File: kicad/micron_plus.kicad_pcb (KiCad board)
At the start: 2 copper layers, 163.8 x 123.2 mm, 90 parts, among them J1 Conn_02x17_Odd_Even, J2 Cliff DC10A, Q1 2N2905A, Q2 2N2905A, Q3 2N3904, Q4 2N3904, U1 MC68A21, U10 74LS00, U11 7406, U12 HM6264LP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

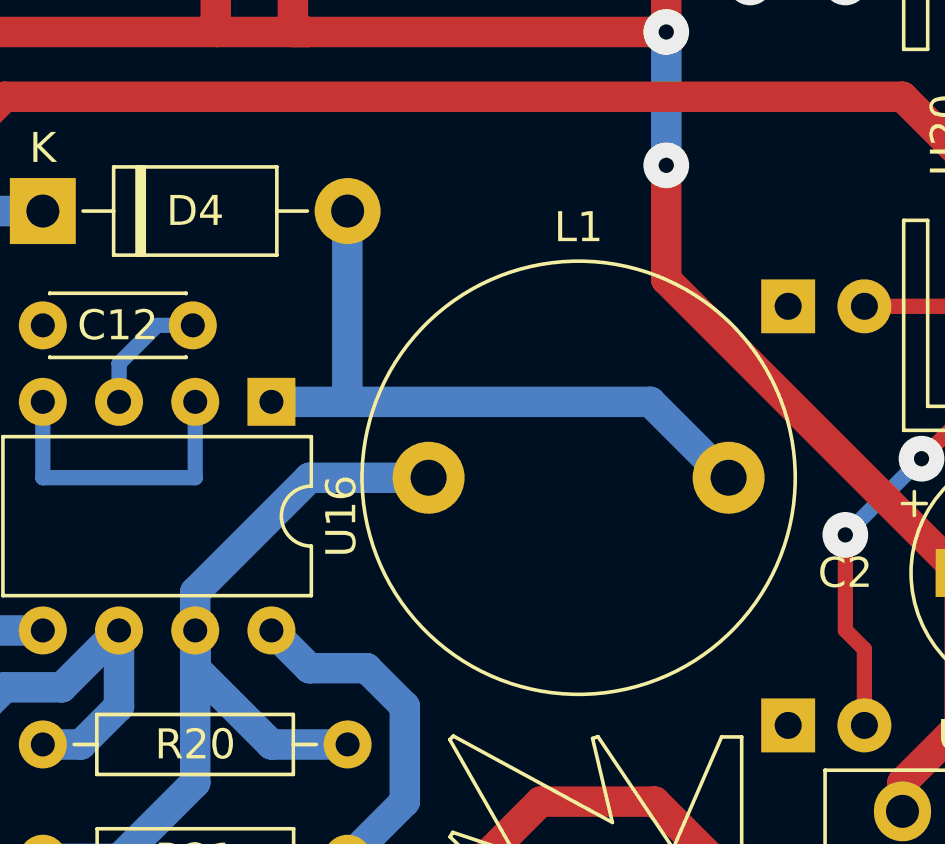
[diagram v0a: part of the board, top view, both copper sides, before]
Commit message: KiCAD: Custom footprint for inductor with multiple pads
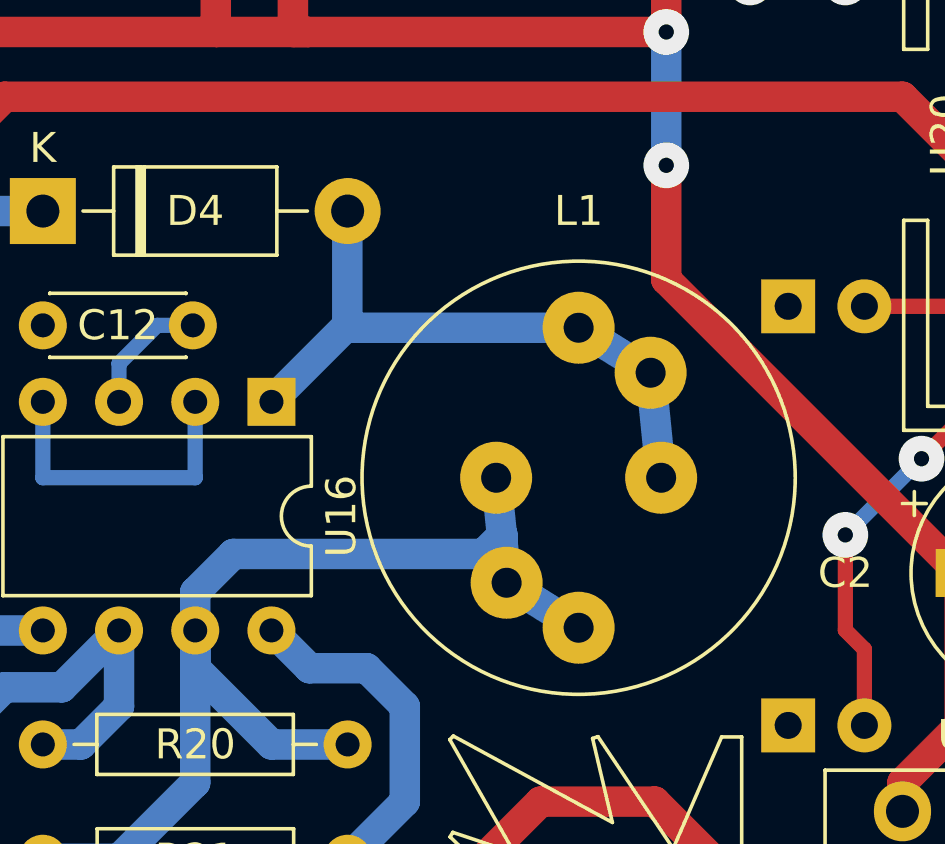
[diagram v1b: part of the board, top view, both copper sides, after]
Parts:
- L1: footprint Inductor_THT:L_Radial_D14.2mm_P10.00mm_Neosid_SD14 -> custom_footprints:L_Radial_D14.2mm_P10.00mm_Kemet
- moved L1 7.07 mm to (159.4, 127.6), turned to 90 degrees
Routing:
- net Net-(L1-Pad1): track 29.2 -> 38.7 mm
- net Net-(D4-Pad2): track 22.6 -> 21.5 mm
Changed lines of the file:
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@@
     )
   )
-  (footprint "Inductor_THT:L_Radial_D14.2mm_P10.00mm_Neosid_SD14" (layer "F.Cu")
-    (at 154.385 122.555)
+  (footprint "custom_footprints:L_Radial_D14.2mm_P10.00mm_Kemet" (layer "F.Cu")
+    (at 159.385 127.555 90)
     (descr "Inductor, Radial series, Radial, pin pitch=10.00mm, , diameter=14.2mm, Neosid, SD14, http://www.neosid.de/produktblaetter/neosid_Festinduktivitaet_Sd14.pdf")
     (tags "Inductor Radial series Radial pin pitch 10.00mm  diameter 14.2mm Neosid SD14")
@@
     (property "Sheetname" "Power Supply")
     (attr through_hole)
-    (fp_text reference "L1" (at 5 -8.35) (layer "F.SilkS")
+    (fp_text reference "L1" (at 13.89 0 180) (layer "F.SilkS")
       (effects (font (size 1 1) (thickness 0.15)))
     )
-    (fp_text value "220uH" (at 5 8.35) (layer "F.Fab")
+    (fp_text value "220uH" (at 5 8.35 90) (layer "F.Fab")
       (effects (font (size 1 1) (thickness 0.15)))
     )
-    (fp_text user "${REFERENCE}" (at 5 0) (layer "F.Fab")
+    (fp_text user "${REFERENCE}" (at 5 -5 90) (layer "F.Fab")
       (effects (font (size 1 1) (thickness 0.15)))
     )
@@
     (fp_circle (center 5 0) (end 12.35 0) (layer "F.CrtYd") (width 0.05) (fill none))
     (fp_circle (center 5 0) (end 12.1 0) (layer "F.Fab") (width 0.1) (fill none))
-    (pad "1" thru_hole circle (at 0 0) (size 2.4 2.4) (drill 1.2) (layers *.Cu *.Mask)
+    (pad "1" thru_hole circle (at 1.5 -2.4 90) (size 2.4 2.4) (drill 1) (layers *.Cu *.Mask)
       (net 174 "Net-(L1-Pad1)") (pinfunction "1") (pintype "passive"))
-    (pad "2" thru_hole circle (at 10 0) (size 2.4 2.4) (drill 1.2) (layers *.Cu *.Mask)
+    (pad "1" thru_hole circle (at 5 -2.75 90) (size 2.4 2.4) (drill 1) (layers *.Cu *.Mask)
+      (net 174 "Net-(L1-Pad1)") (pinfunction "1") (pintype "passive"))
+    (pad "1" thru_hole circle (at 0 0 90) (size 2.4 2.4) (drill 1) (layers *.Cu *.Mask)
+      (net 174 "Net-(L1-Pad1)") (pinfunction "1") (pintype "passive"))
+    (pad "2" thru_hole circle (at 10 0 90) (size 2.4 2.4) (drill 1) (layers *.Cu *.Mask)
+      (net 173 "Net-(D4-Pad2)") (pinfunction "2") (pintype "passive"))
+    (pad "2" thru_hole circle (at 5 2.75 90) (size 2.4 2.4) (drill 1) (layers *.Cu *.Mask)
+      (net 173 "Net-(D4-Pad2)") (pinfunction "2") (pintype "passive"))
+    (pad "2" thru_hole circle (at 8.5 2.4 90) (size 2.4 2.4) (drill 1) (layers *.Cu *.Mask)
       (net 173 "Net-(D4-Pad2)") (pinfunction "2") (pintype "passive"))
     (model "${KICAD6_3DMODEL_DIR}/Inductor_THT.3dshapes/L_Radial_D14.2mm_P10.00mm_Neosid_SD14.wrl"
@@
   (segment (start 77.724 33.528) (end 81.026 36.83) (width 0.508) (layer "B.Cu") (net 169))
   (segment (start 58.928 35.56) (end 58.928 35.052) (width 0.508) (layer "B.Cu") (net 169))
-  (segment (start 151.675 120.025) (end 151.675 113.675) (width 1.016) (layer "B.Cu") (net 173))
-  (segment (start 149.145 120.025) (end 151.675 120.025) (width 1.016) (layer "B.Cu") (net 173))
-  (segment (start 151.675 120.025) (end 161.775 120.025) (width 1.016) (layer "B.Cu") (net 173))
-  (segment (start 161.775 120.025) (end 164.305 122.555) (width 1.016) (layer "B.Cu") (net 173))
-  (segment (start 146.605 126.365) (end 146.605 127.645) (width 1.016) (layer "B.Cu") (net 174))
+  (segment (start 159.385 117.555) (end 151.755 117.555) (width 1.016) (layer "B.Cu") (net 173))
+  (segment (start 162.135 122.555) (end 161.785 119.055) (width 1.016) (layer "B.Cu") (net 173))
+  (segment (start 149.145 120.005) (end 151.675 117.475) (width 1.016) (layer "B.Cu") (net 173))
+  (segment (start 159.385 117.555) (end 161.785 119.055) (width 1.016) (layer "B.Cu") (net 173))
+  (segment (start 151.675 117.475) (end 151.675 113.675) (width 1.016) (layer "B.Cu") (net 173))
+  (segment (start 151.755 117.555) (end 151.675 117.475) (width 1.016) (layer "B.Cu") (net 173))
+  (segment (start 156.21 125.095) (end 156.845 124.46) (width 1.016) (layer "B.Cu") (net 174))
+  (segment (start 156.845 124.46) (end 156.845 125.915) (width 1.016) (layer "B.Cu") (net 174))
   (segment (start 146.605 127.645) (end 146.605 132.715) (width 1.016) (layer "B.Cu") (net 174))
   (segment (start 149.145 131.445) (end 146.605 128.905) (width 1.016) (layer "B.Cu") (net 174))
-  (segment (start 154.385 122.555) (end 150.415 122.555) (width 1.016) (layer "B.Cu") (net 174))
+  (segment (start 146.605 127.645) (end 146.605 126.365) (width 1.016) (layer "B.Cu") (net 174))
+  (segment (start 156.635 122.555) (end 156.985 126.055) (width 1.016) (layer "B.Cu") (net 174))
   (segment (start 144.065 135.255) (end 141.525 135.255) (width 1.016) (layer "B.Cu") (net 174))
-  (segment (start 150.415 122.555) (end 146.605 126.365) (width 1.016) (layer "B.Cu") (net 174))
   (segment (start 151.685 131.445) (end 149.145 131.445) (width 1.016) (layer "B.Cu") (net 174))
   (segment (start 146.605 128.905) (end 146.605 127.635) (width 1.016) (layer "B.Cu") (net 174))
+  (segment (start 147.875 125.095) (end 156.21 125.095) (width 1.016) (layer "B.Cu") (net 174))
+  (segment (start 146.605 126.365) (end 147.875 125.095) (width 1.016) (layer "B.Cu") (net 174))
+  (segment (start 156.985 126.055) (end 159.385 127.555) (width 1.016) (layer "B.Cu") (net 174))
   (segment (start 146.605 132.715) (end 144.065 135.255) (width 1.016) (layer "B.Cu") (net 174))
   (segment (start 191.77 71.11) (end 191.77 68.57) (width 0.508) (layer "F.Cu") (net 175))
@@
   (segment (start 189.23 93.345) (end 187.96 92.075) (width 0.508) (layer "B.Cu") (net 182))
   (zone (net 2) (net_name "GND") (layer "B.Cu") (hatch edge 0.508)
-    (connect_pads (clearance 1.27))
+    (connect_pads (clearance 1.016))
     (min_thickness 0.508) (filled_areas_thickness no)
     (fill yes (thermal_gap 0.508) (thermal_bridge_width 0.508))

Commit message: KiCAD - silk screen
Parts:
- C11, C13: value 100u/50V -> 100u
- C15: value 4.7u/35V -> 4u7
- C2: value 220u/16V -> 220u
- C8: value 10u/35V -> 10u
- C9: value 100u/16V -> 100u
- U18: value LM7805_TO220 -> LM7805
- U19, U20: value LM317SP_TO220 -> LM317T
- moved C15 0.71 mm to (185.4, 85.7)
- moved R20 0.64 mm to (141.5, 132.1)
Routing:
- net Net-(C15-Pad1): track 67.1 -> 65.4 mm
- net Net-(C16-Pad1): track 58.2 -> 56.7 mm
- net Net-(U10-Pad4): track 133.4 -> 134.7 mm
- net GND: track 681.7 -> 682.7 mm
- net /Main Logic and Eprom Socket/EpromVPP: track 180.0 -> 179.1 mm
- net /Control Latches/n2564Mode: track 127.3 -> 126.7 mm
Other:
- board text added: "16V"
- board text added: "35V"
- board text added: "50V"
- board text added: "9VDC Centre+"

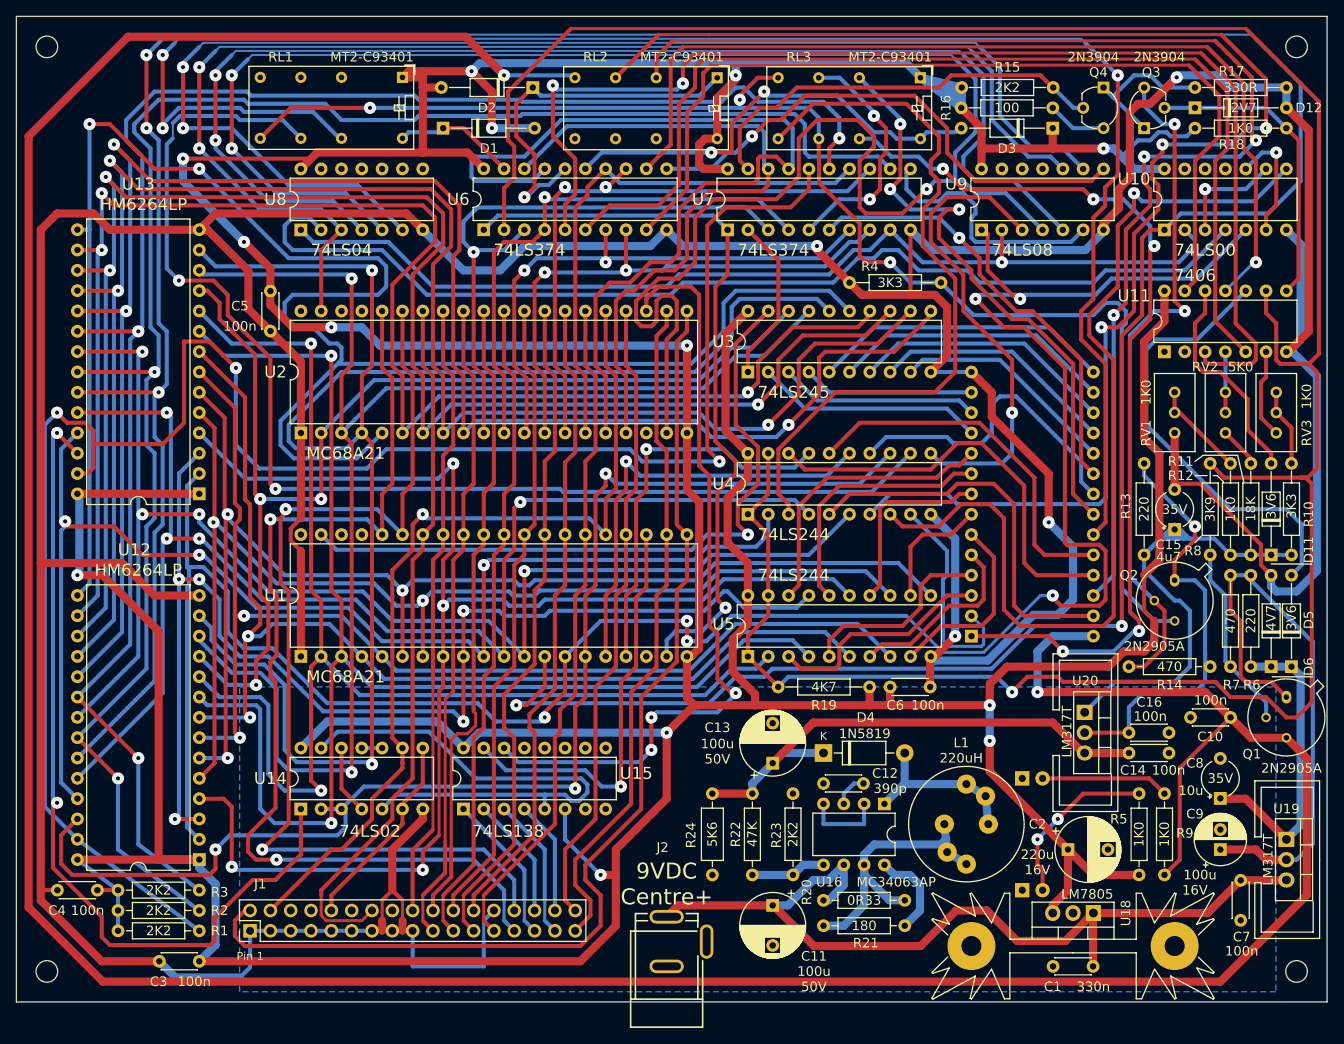
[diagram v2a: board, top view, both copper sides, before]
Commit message: KiCAD - more silk screen
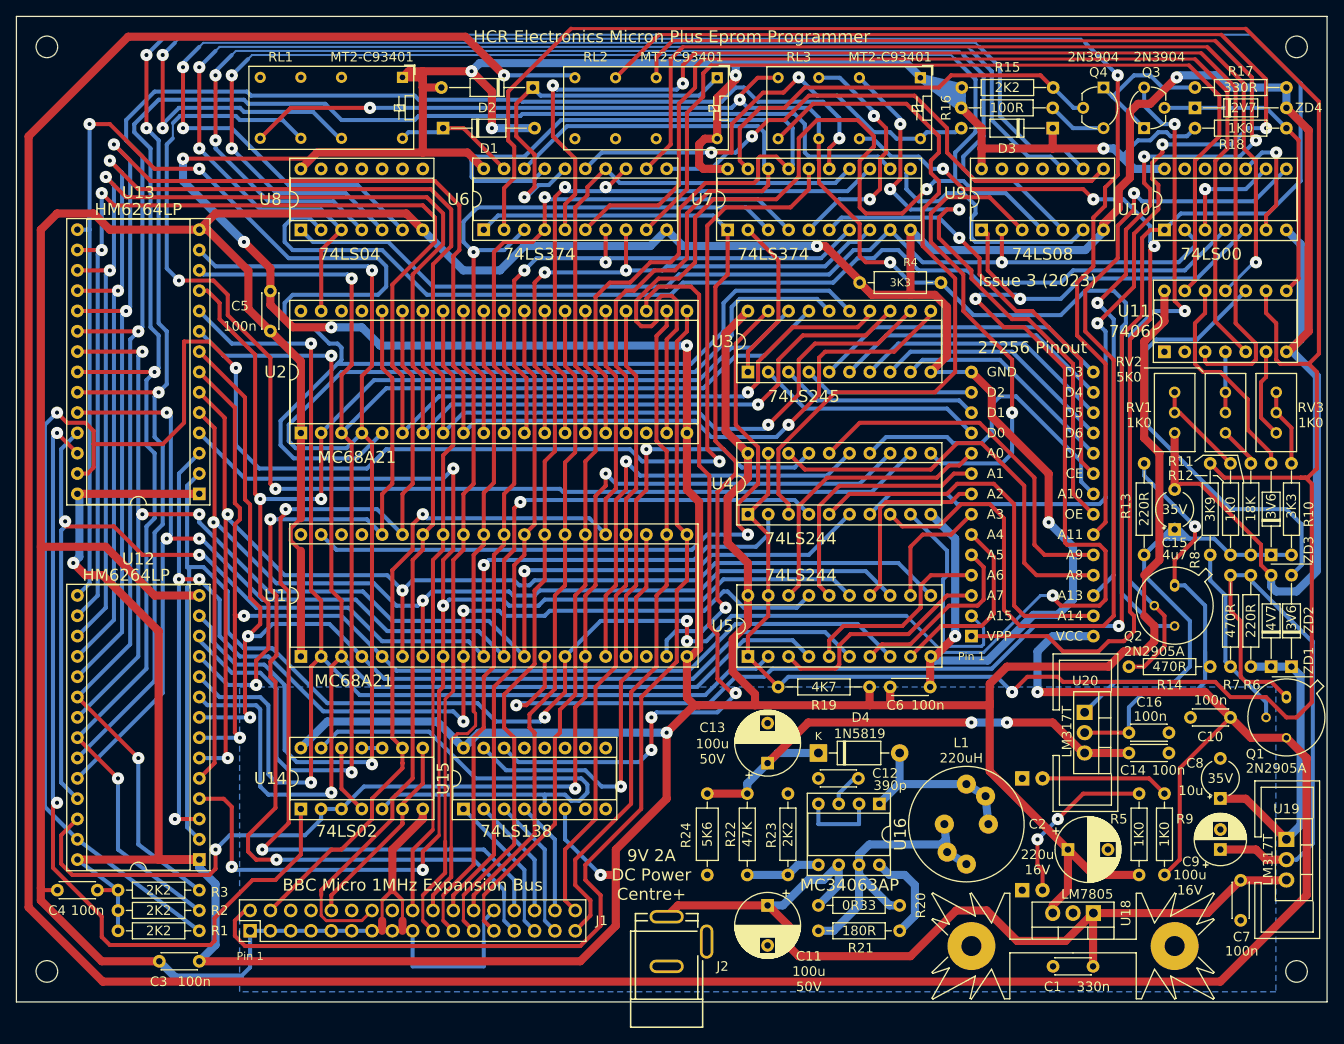
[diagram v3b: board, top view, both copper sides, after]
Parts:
- R13, R6: value 220 -> 220R
- R14, R7: value 470 -> 470R
- R16: value 100 -> 100R
- R21: value 180 -> 180R
- R4: footprint custom_footprints:R_Axial_DIN0207_L6.3mm_D2.0mm_P11.43mm_Horizontal -> Resistor_THT:R_Axial_DIN0207_L6.3mm_D2.5mm_P10.16mm_Horizontal
- U1, U2: footprint Package_DIP:DIP-40_W15.24mm -> Package_DIP:DIP-40_W15.24mm_Socket
- U10, U11, U14, U8, U9: footprint Package_DIP:DIP-14_W7.62mm -> Package_DIP:DIP-14_W7.62mm_Socket
- U12, U13: footprint Package_DIP:DIP-28_W15.24mm -> Package_DIP:DIP-28_W15.24mm_Socket
- U15: footprint Package_DIP:DIP-16_W7.62mm -> Package_DIP:DIP-16_W7.62mm_Socket
- U16: footprint Package_DIP:DIP-8_W7.62mm -> Package_DIP:DIP-8_W7.62mm_Socket
- U3, U4, U5, U6, U7: footprint Package_DIP:DIP-20_W7.62mm -> Package_DIP:DIP-20_W7.62mm_Socket
- moved C12 0.90 mm to (145.9, 116.8)
- moved R20 0.90 mm to (140.9, 132.7)
- moved R21 0.90 mm to (151.1, 135.9)
- moved C11 0.64 mm to (134.5, 132.7)
- moved C13 0.64 mm to (134.5, 114.9)
- moved D4 0.64 mm to (140.9, 113.7)
- moved U16 0.64 mm to (148.5, 120.0)
- moved R24 0.64 mm to (127.0, 128.9)
- moved Q2 0.63 mm to (185.4, 92.7)
- moved R22 0.63 mm to (132.0, 128.9)
- moved R23 0.63 mm to (137.1, 118.7)
- renumbered D10 to LED1, D7 to LED2, D6 to ZD1, D5 to ZD2, D11 to ZD3, D12 to ZD4
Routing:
- net /1MHz Bus and PIA Interface/Addr1: track 170.8 -> 164.0 mm
- net /1MHz Bus and PIA Interface/Addr13: track 160.6 -> 156.7 mm
- net /1MHz Bus and PIA Interface/Addr0: track 159.2 -> 156.0 mm
- net /Power Supply/9VDC: track 110.0 -> 112.8 mm
- net /Main Logic and Eprom Socket/EpromVPP: track 179.1 -> 181.4 mm
- net /Main Logic and Eprom Socket/Eprom26VCC: track 160.7 -> 162.4 mm
- net /Control Latches/nRelay3: track 55.8 -> 57.3 mm
- net Net-(L1-Pad1): track 39.0 -> 40.1 mm
- net /1MHz Bus and PIA Interface/Addr6: track 176.9 -> 176.0 mm
- net /Main Logic and Eprom Socket/Eprom1VPP: track 116.2 -> 115.3 mm, vias 5 -> 3
- net /Main Logic and Eprom Socket/Eprom26: track 186.5 -> 185.7 mm
- net Net-(C16-Pad1): track 56.7 -> 55.9 mm
- net /Power Supply/28VDC: track 65.0 -> 65.6 mm, vias 0 -> 2
- net Net-(R21-Pad1): track 11.4 -> 12.0 mm
- net Net-(D4-Pad2): track 21.5 -> 22.1 mm
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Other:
- board text added: "27256 Pinout"
- board text added: "9V 2A DC Power Centre+"
- board text added: "A0"
- board text added: "A1"
- board text added: "A10"
- board text added: "A11"
- board text added: "A13"
- board text added: "A14"
- board text added: "A15"
- board text added: "A2"
- board text added: "A3"
- board text added: "A4"
- board text added: "A5"
- board text added: "A6"
- board text added: "A7"
- board text added: "A8"
- board text added: "A9"
- board text added: "BBC Micro 1MHz Expansion Bus"
- board text added: "CE"
- board text added: "D0"
- board text added: "D1"
- board text added: "D2"
- board text added: "D3"
- board text added: "D4"
- board text added: "D5"
- board text added: "D6"
- board text added: "D7"
- board text added: "GND"
- board text added: "HCR Electronics Micron Plus Eprom Programmer"
- board text added: "Issue 3 (2023)"
- board text added: "OE"
- board text added: "VCC"
- board text added: "VPP"
- board text removed: "9VDC Centre+"

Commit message: KiCAD: Customize IC footprint silk screen
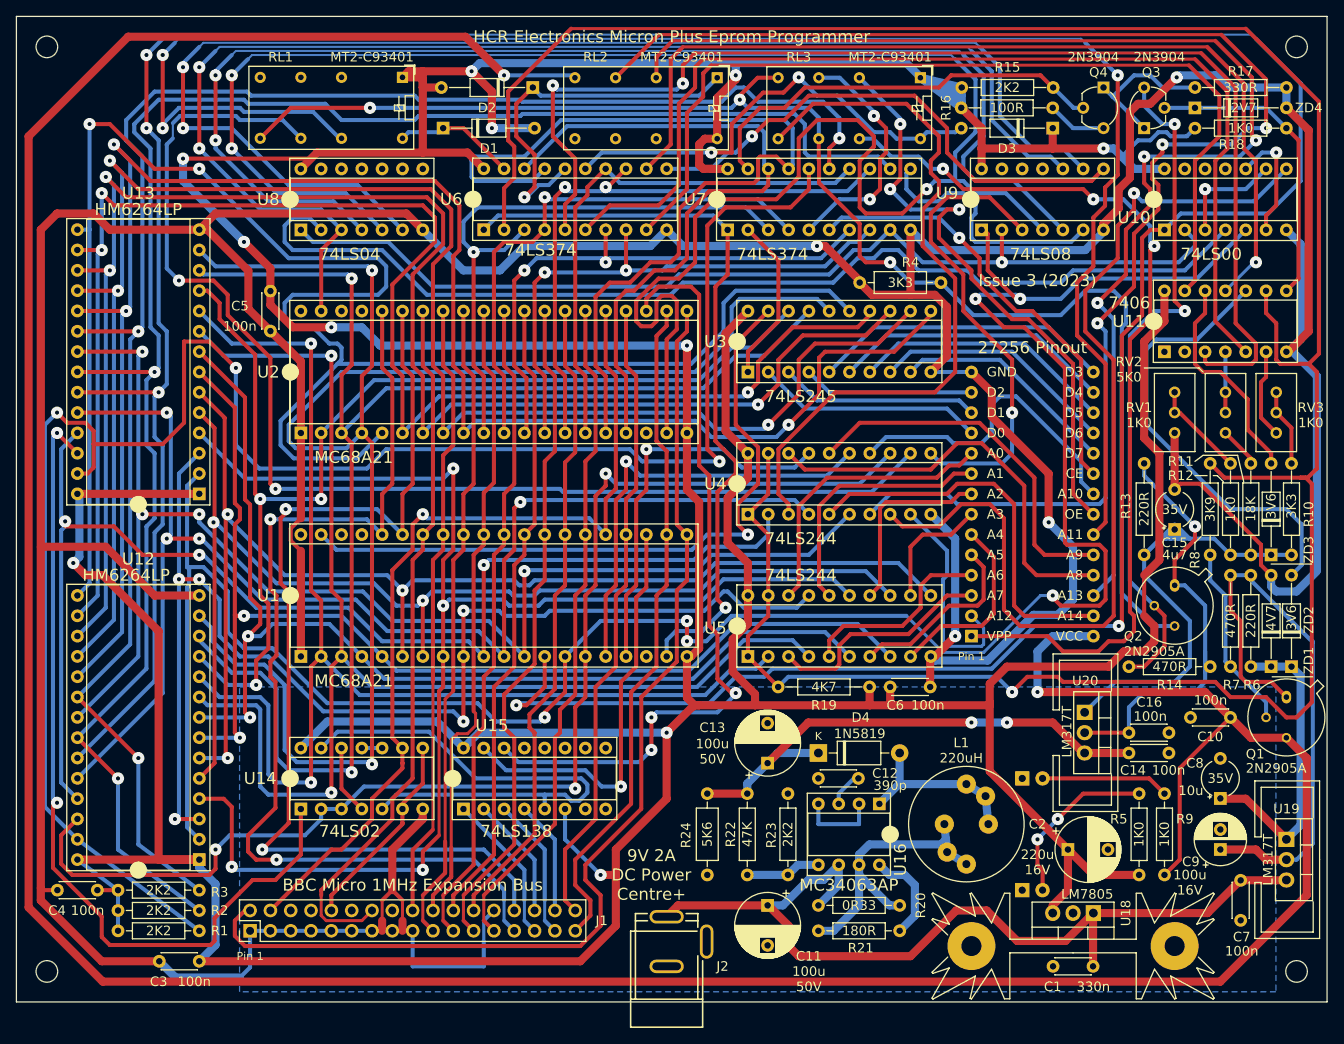
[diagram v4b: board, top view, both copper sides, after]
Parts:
- U1, U2: footprint Package_DIP:DIP-40_W15.24mm_Socket -> custom_footprints:DIP-40_W15.24mm_Socket
- U10, U11, U14, U8, U9: footprint Package_DIP:DIP-14_W7.62mm_Socket -> custom_footprints:DIP-14_W7.62mm_Socket
- U12, U13: footprint Package_DIP:DIP-28_W15.24mm_Socket -> custom_footprints:DIP-28_W15.24mm_Socket
- U15: footprint Package_DIP:DIP-16_W7.62mm_Socket -> custom_footprints:DIP-16_W7.62mm_Socket
- U16: footprint Package_DIP:DIP-8_W7.62mm_Socket -> custom_footprints:DIP-8_W7.62mm_Socket
- U3, U4, U5, U6, U7: footprint Package_DIP:DIP-20_W7.62mm_Socket -> custom_footprints:DIP-20_W7.62mm_Socket
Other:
- board text added: "A12"
- board text removed: "A15"
